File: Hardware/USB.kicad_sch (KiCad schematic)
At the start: 14 parts, among them J5 USB4120-03-C, U8 CP2102N-A02-GQFN24

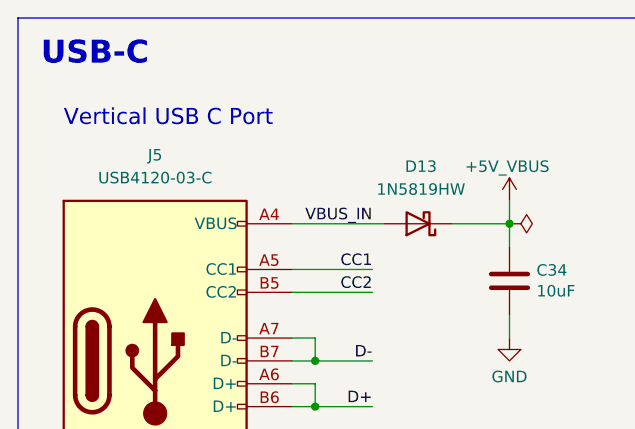
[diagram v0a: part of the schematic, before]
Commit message: differential amp for LPF
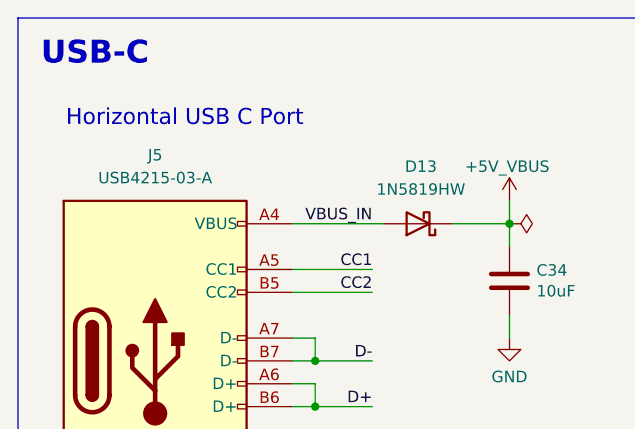
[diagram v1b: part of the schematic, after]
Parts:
- J5: value USB4120-03-C -> USB4215-03-A; footprint Parts:USB412003C -> UTSVT_Connectors:USB_C_Receptacle_GCT_USB4105-xx-A_16P_TopMnt_Horizontal; P/N USB4120-03-C -> USB4215-03-A
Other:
- note added: "Horizontal USB C Port"
- note removed: "Vertical USB C Port"
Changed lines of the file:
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@@
 		)
 	)
-	(text "Vertical USB C Port"
-		(exclude_from_sim no)
-		(at 20.32 25.4 0)
+	(text "Horizontal USB C Port"
+		(exclude_from_sim no)
+		(at 20.574 25.4 0)
 		(effects
 			(font
@@
 			)
 		)
-		(property "Value" "USB4120-03-C"
+		(property "Value" "USB4215-03-A"
 			(at 30.48 33.02 0)
 			(effects
@@
 			)
 		)
-		(property "Footprint" "Parts:USB412003C"
+		(property "Footprint" "UTSVT_Connectors:USB_C_Receptacle_GCT_USB4105-xx-A_16P_TopMnt_Horizontal"
 			(at 34.29 53.34 0)
 			(effects
@@
 			)
 		)
-		(property "Datasheet" "https://www.mouser.com/catalog/specsheets/GCT_USB4120.pdf"
+		(property "Datasheet" "https://www.mouser.com/datasheet/2/837/usb4215-3472997.pdf"
 			(at 34.29 53.34 0)
 			(effects
@@
 			)
 		)
-		(property "P/N" "USB4120-03-C"
+		(property "P/N" "USB4215-03-A "
 			(at 30.48 53.34 0)
 			(effects

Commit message: new TLV symbol, SPDT switch for scrut
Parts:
- J5: P/N USB4215-03-A -> USB4215-03-A
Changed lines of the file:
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@@
 			)
 		)
-		(property "P/N" "USB4215-03-A "
+		(property "P/N" "USB4215-03-A"
 			(at 30.48 53.34 0)
 			(effects

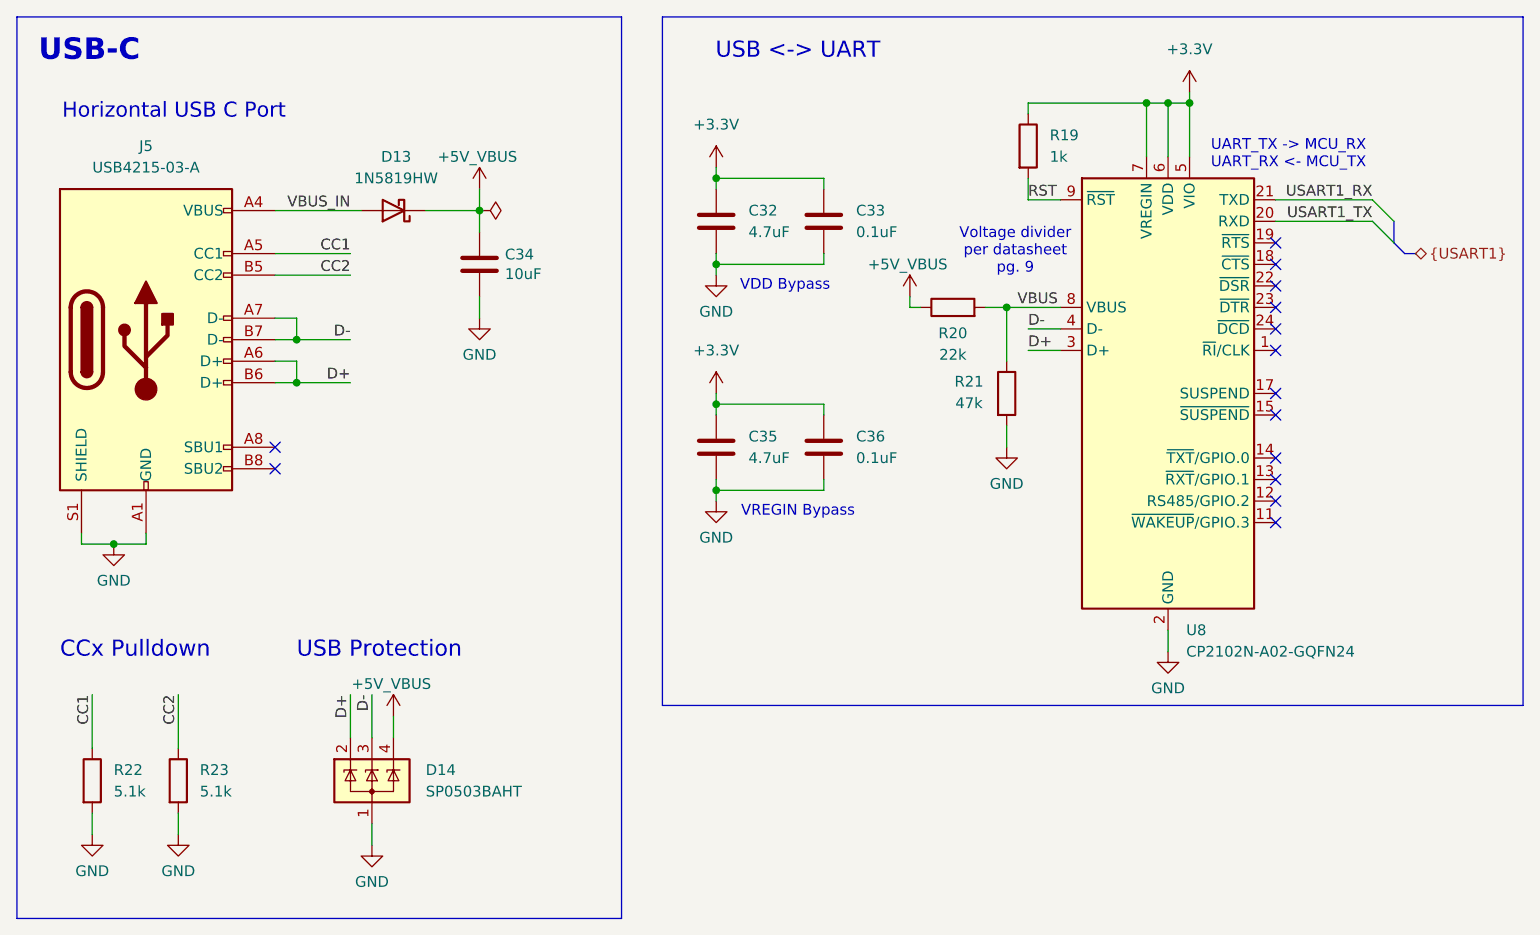
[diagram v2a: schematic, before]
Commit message: refactored and added LPF docs; added fuse, boot_gpio from USB-UART chip
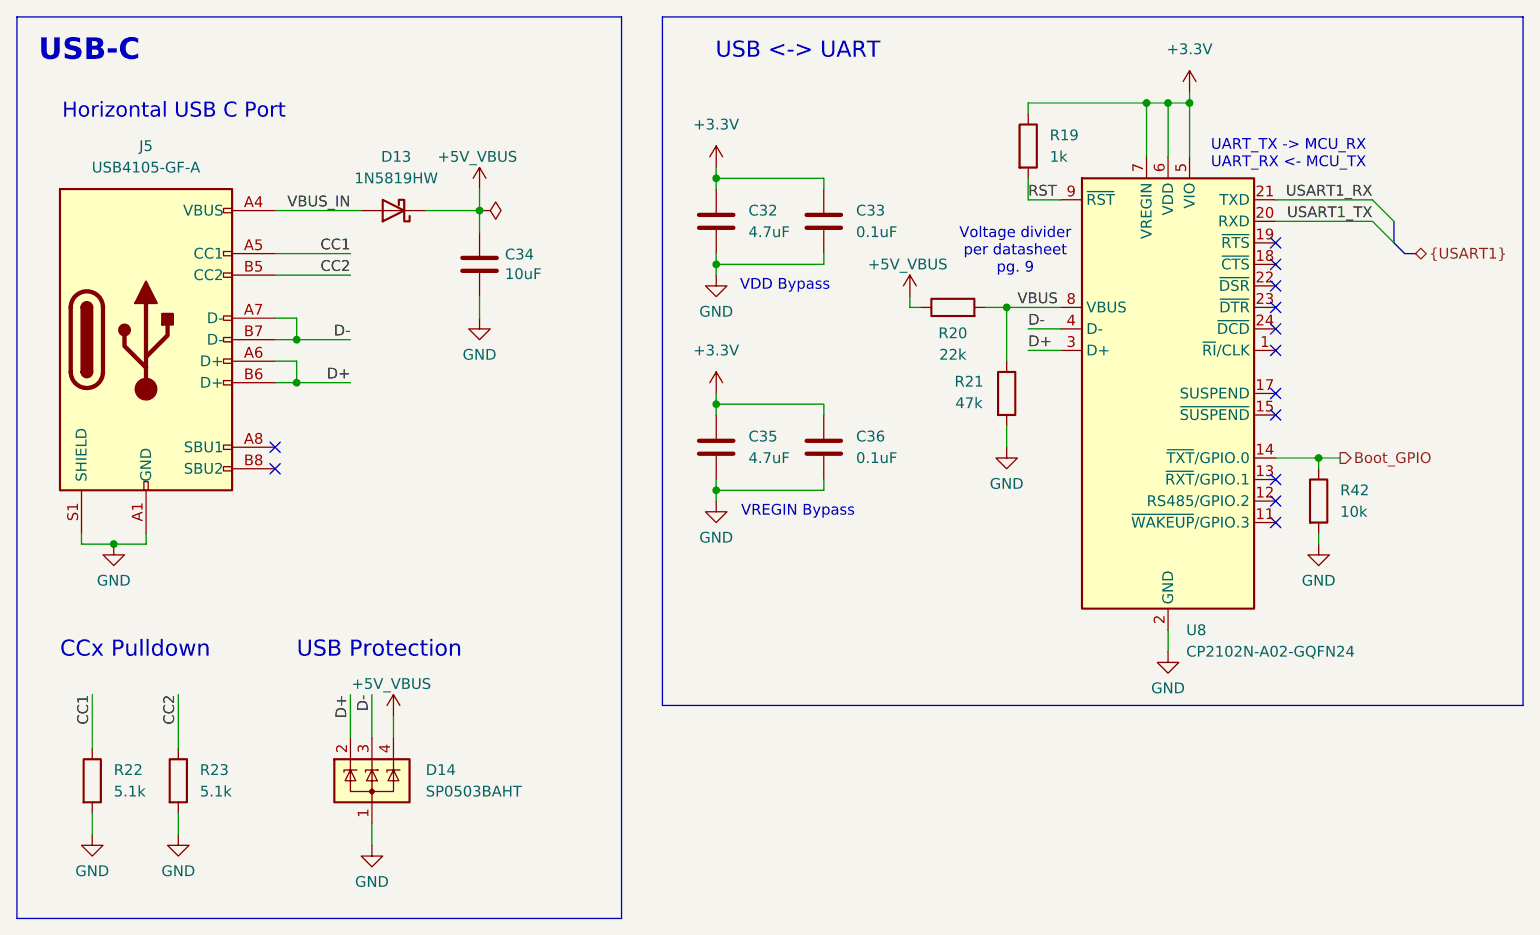
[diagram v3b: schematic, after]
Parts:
- added R42: 10k, symbol Device:R
- J5: value USB4215-03-A -> USB4105-GF-A; P/N USB4215-03-A -> USB4105-GF-A
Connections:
- net GND: now also R42.2
- net Boot_GPIO: now reaches U8.14 (~{TXT}/GPIO.0)
- net Boot_GPIO: now also R42.1
- no-connect marks 14 -> 13
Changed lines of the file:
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@@
+	)
+	(junction
+		(at 168.91 67.31)
+		(diameter 0)
+		(color 0 0 0 0)
 	)
 	(junction
@@
 	)
 	(no_connect
-		(at 163.83 67.31)
-	)
-	(no_connect
 		(at 163.83 49.53)
 	)
@@
 	(wire
 		(pts
+			(xy 163.83 67.31) (xy 168.91 67.31)
+		)
+		(stroke
+			(width 0)
+			(type default)
+		)
+	)
+	(wire
+		(pts
 			(xy 45.72 53.34) (xy 48.26 53.34)
 		)
@@
 	(wire
 		(pts
+			(xy 168.91 68.58) (xy 168.91 67.31)
+		)
+		(stroke
+			(width 0)
+			(type default)
+		)
+	)
+	(wire
+		(pts
 			(xy 120.65 49.53) (xy 121.92 49.53)
 		)
@@
 		)
 	)
+	(wire
+		(pts
+			(xy 168.91 77.47) (xy 168.91 76.2)
+		)
+		(stroke
+			(width 0)
+			(type default)
+		)
+	)
 	(bus
 		(pts
@@
 		(pts
 			(xy 148.59 25.4) (xy 151.13 25.4)
+		)
+		(stroke
+			(width 0)
+			(type default)
+		)
+	)
+	(wire
+		(pts
+			(xy 168.91 67.31) (xy 171.45 67.31)
 		)
 		(stroke
@@
 		(shape bidirectional)
 		(at 180.34 43.18 0)
+		(effects
+			(font
+				(size 1.27 1.27)
+			)
+			(justify left)
+		)
+	)
+	(hierarchical_label "Boot_GPIO"
+		(shape output)
+		(at 171.45 67.31 0)
 		(effects
 			(font
@@
 	)
 	(symbol
+		(lib_id "Device:R")
+		(at 168.91 72.39 0)
+		(unit 1)
+		(exclude_from_sim no)
+		(in_bom yes)
+		(on_board yes)
+		(dnp no)
+		(fields_autoplaced yes)
+		(property "Reference" "R42"
+			(at 171.45 71.1199 0)
+			(effects
+				(font
+					(size 1.27 1.27)
+				)
+				(justify left)
+			)
+		)
+		(property "Value" "10k"
+			(at 171.45 73.6599 0)
+			(effects
+				(font
+					(size 1.27 1.27)
+				)
+				(justify left)
+			)
+		)
+		(property "Footprint" ""
+			(at 167.132 72.39 90)
+			(effects
+				(font
+					(size 1.27 1.27)
+				)
+				(hide yes)
+			)
+		)
+		(property "Datasheet" "~"
+			(at 168.91 72.39 0)
+			(effects
+				(font
+					(size 1.27 1.27)
+				)
+				(hide yes)
+			)
+		)
+		(property "Description" "Resistor"
+			(at 168.91 72.39 0)
+			(effects
+				(font
+					(size 1.27 1.27)
+				)
+				(hide yes)
+			)
+		)
+		(pin "1"
+		)
+		(pin "2"
+		)
+		(instances
+			(project ""
+				(path "/a452d214-ea00-440d-a445-5d6103fda43a/c14a2c5c-255b-423f-b086-532f80606e87"
+					(reference "R42")
+					(unit 1)
+				)
+			)
+		)
+	)
+	(symbol
 		(lib_id "power:+24V")
 		(at 69.85 35.56 0)
@@
 				(path "/a452d214-ea00-440d-a445-5d6103fda43a/c14a2c5c-255b-423f-b086-532f80606e87"
 					(reference "#PWR084")
+					(unit 1)
+				)
+			)
+		)
+	)
+	(symbol
+		(lib_id "power:GND")
+		(at 168.91 77.47 0)
+		(unit 1)
+		(exclude_from_sim no)
+		(in_bom yes)
+		(on_board yes)
+		(dnp no)
+		(property "Reference" "#PWR0113"
+			(at 168.91 83.82 0)
+			(effects
+				(font
+					(size 1.27 1.27)
+				)
+				(hide yes)
+			)
+		)
+		(property "Value" "GND"
+			(at 168.91 81.788 0)
+			(effects
+				(font
+					(size 1.27 1.27)
+				)
+			)
+		)
+		(property "Footprint" ""
+			(at 168.91 77.47 0)
+			(effects
+				(font
+					(size 1.27 1.27)
+				)
+				(hide yes)
+			)
+		)
+		(property "Datasheet" ""
+			(at 168.91 77.47 0)
+			(effects
+				(font
+					(size 1.27 1.27)
+				)
+				(hide yes)
+			)
+		)
+		(property "Description" "Power symbol creates a global label with name \"GND\" , ground"
+			(at 168.91 77.47 0)
+			(effects
+				(font
+					(size 1.27 1.27)
+				)
+				(hide yes)
+			)
+		)
+		(pin "1"
+		)
+		(instances
+			(project "PS-AmperesPCB"
+				(path "/a452d214-ea00-440d-a445-5d6103fda43a/c14a2c5c-255b-423f-b086-532f80606e87"
+					(reference "#PWR0113")
 					(unit 1)
 				)
@@
 			)
 		)
-		(property "Value" "USB4215-03-A"
+		(property "Value" "USB4105-GF-A"
 			(at 30.48 33.02 0)
 			(effects
@@
 			)
 		)
-		(property "Datasheet" "https://www.mouser.com/datasheet/2/837/usb4215-3472997.pdf"
+		(property "Datasheet" "https://www.mouser.com/ProductDetail/GCT/USB4105-GF-A?qs=KUoIvG%2F9IlY%2FMLlBMpStpA%3D%3D"
 			(at 34.29 53.34 0)
 			(effects
@@
 			)
 		)
-		(property "P/N" "USB4215-03-A"
+		(property "P/N" "USB4105-GF-A"
 			(at 30.48 53.34 0)
 			(effects

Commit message: slightly cooked
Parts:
- R42: footprint (none) -> Resistor_SMD:R_0603_1608Metric_Pad0.98x0.95mm_HandSolder
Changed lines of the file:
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@@
 			)
 		)
-		(property "Footprint" ""
+		(property "Footprint" "Resistor_SMD:R_0603_1608Metric_Pad0.98x0.95mm_HandSolder"
 			(at 167.132 72.39 90)
 			(effects

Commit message: layout stuff
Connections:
- net D+: now also D14.3 (K); no longer D14.2 (K)
- net D-: now also D14.2 (K); no longer D14.3 (K)
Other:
- note added: "Enable bootloader using CP2102N GPIO"
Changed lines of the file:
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@@
+		)
+	)
+	(text "Enable bootloader \nusing CP2102N GPIO"
+		(exclude_from_sim no)
+		(at 169.164 61.722 0)
+		(effects
+			(font
+				(size 1.27 1.27)
+			)
+			(justify left top)
 		)
 	)
@@
 	)
 	(label "D+"
-		(at 54.61 95.25 270)
+		(at 57.15 95.25 270)
 		(effects
 			(font
@@
 	)
 	(label "D-"
-		(at 57.15 95.25 270)
-		(effects
-			(font
+		(at 54.61 95.25 270)
+		(effects
+			(font

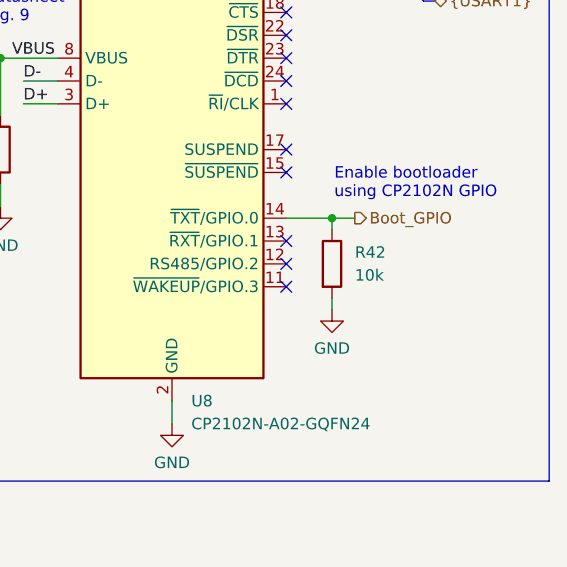
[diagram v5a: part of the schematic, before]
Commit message: post review council sch changes: shielded connectors, removed SHDN resistor, diode OR for boot, standardized resistors
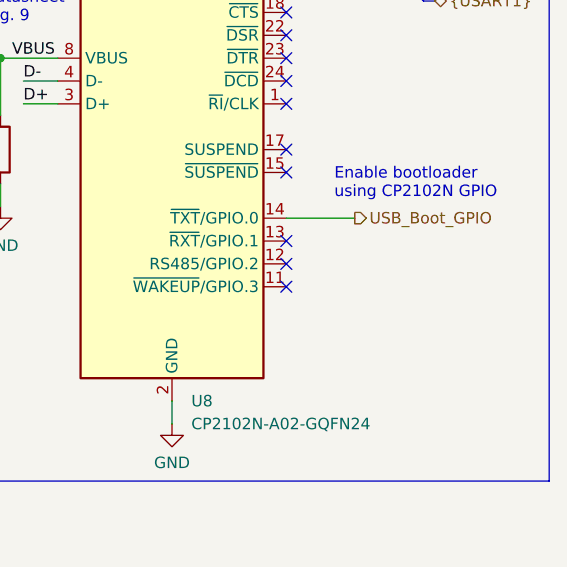
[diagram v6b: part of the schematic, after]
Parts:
- removed R42: 10k, Resistor_SMD:R_0603_1608Metric_Pad0.98x0.95mm_HandSolder, symbol Device:R
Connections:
- net Boot_GPIO renamed USB_Boot_GPIO
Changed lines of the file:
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@@
-	)
-	(junction
-		(at 168.91 67.31)
-		(diameter 0)
-		(color 0 0 0 0)
 	)
 	(junction
@@
 	(wire
 		(pts
-			(xy 163.83 67.31) (xy 168.91 67.31)
+			(xy 163.83 67.31) (xy 171.45 67.31)
 		)
 		(stroke
@@
 	(wire
 		(pts
-			(xy 168.91 68.58) (xy 168.91 67.31)
-		)
-		(stroke
-			(width 0)
-			(type default)
-		)
-	)
-	(wire
-		(pts
 			(xy 120.65 49.53) (xy 121.92 49.53)
 		)
@@
 		)
 	)
-	(wire
-		(pts
-			(xy 168.91 77.47) (xy 168.91 76.2)
-		)
-		(stroke
-			(width 0)
-			(type default)
-		)
-	)
 	(bus
 		(pts
@@
 		(pts
 			(xy 148.59 25.4) (xy 151.13 25.4)
-		)
-		(stroke
-			(width 0)
-			(type default)
-		)
-	)
-	(wire
-		(pts
-			(xy 168.91 67.31) (xy 171.45 67.31)
 		)
 		(stroke
@@
 		)
 	)
-	(hierarchical_label "Boot_GPIO"
+	(hierarchical_label "USB_Boot_GPIO"
 		(shape output)
 		(at 171.45 67.31 0)
@@
 	)
 	(symbol
-		(lib_id "Device:R")
-		(at 168.91 72.39 0)
-		(unit 1)
-		(exclude_from_sim no)
-		(in_bom yes)
-		(on_board yes)
-		(dnp no)
-		(fields_autoplaced yes)
-		(property "Reference" "R42"
-			(at 171.45 71.1199 0)
-			(effects
-				(font
-					(size 1.27 1.27)
-				)
-				(justify left)
-			)
-		)
-		(property "Value" "10k"
-			(at 171.45 73.6599 0)
-			(effects
-				(font
-					(size 1.27 1.27)
-				)
-				(justify left)
-			)
-		)
-		(property "Footprint" "Resistor_SMD:R_0603_1608Metric_Pad0.98x0.95mm_HandSolder"
-			(at 167.132 72.39 90)
-			(effects
-				(font
-					(size 1.27 1.27)
-				)
-				(hide yes)
-			)
-		)
-		(property "Datasheet" "~"
-			(at 168.91 72.39 0)
-			(effects
-				(font
-					(size 1.27 1.27)
-				)
-				(hide yes)
-			)
-		)
-		(property "Description" "Resistor"
-			(at 168.91 72.39 0)
-			(effects
-				(font
-					(size 1.27 1.27)
-				)
-				(hide yes)
-			)
-		)
-		(pin "1"
-		)
-		(pin "2"
-		)
-		(instances
-			(project ""
-				(path "/a452d214-ea00-440d-a445-5d6103fda43a/c14a2c5c-255b-423f-b086-532f80606e87"
-					(reference "R42")
-					(unit 1)
-				)
-			)
-		)
-	)
-	(symbol
 		(lib_id "power:+24V")
 		(at 69.85 35.56 0)
@@
 					(unit 1)
 				)
-			)
-		)
-	)
-	(symbol
-		(lib_id "power:GND")
-		(at 168.91 77.47 0)
-		(unit 1)
-		(exclude_from_sim no)
-		(in_bom yes)
-		(on_board yes)
-		(dnp no)
-		(property "Reference" "#PWR0113"
-			(at 168.91 83.82 0)
-			(effects
-				(font
-					(size 1.27 1.27)
-				)
-				(hide yes)
-			)
-		)
-		(property "Value" "GND"
-			(at 168.91 81.788 0)
-			(effects
-				(font
-					(size 1.27 1.27)
-				)
-			)
-		)
-		(property "Footprint" ""
-			(at 168.91 77.47 0)
-			(effects
-				(font
-					(size 1.27 1.27)
-				)
-				(hide yes)
-			)
-		)
-		(property "Datasheet" ""
-			(at 168.91 77.47 0)
-			(effects
-				(font
-					(size 1.27 1.27)
-				)
-				(hide yes)
-			)
-		)
-		(property "Description" "Power symbol creates a global label with name \"GND\" , ground"
-			(at 168.91 77.47 0)
-			(effects
-				(font
-					(size 1.27 1.27)
-				)
-				(hide yes)
-			)
-		)
-		(pin "1"
-		)
-		(instances
-			(project "PS-AmperesPCB"
-				(path "/a452d214-ea00-440d-a445-5d6103fda43a/c14a2c5c-255b-423f-b086-532f80606e87"
-					(reference "#PWR0113")
-					(unit 1)
-				)

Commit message: almost done with routing
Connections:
- net D+: now also D14.2 (K); no longer D14.3 (K)
- net D-: now also D14.3 (K); no longer D14.2 (K)
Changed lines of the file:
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@@
 	)
 	(label "D+"
-		(at 57.15 95.25 270)
+		(at 54.61 95.25 270)
 		(effects
 			(font
@@
 	)
 	(label "D-"
-		(at 54.61 95.25 270)
+		(at 57.15 95.25 270)
 		(effects
 			(font
